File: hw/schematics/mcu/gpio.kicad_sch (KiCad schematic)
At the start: 5 parts

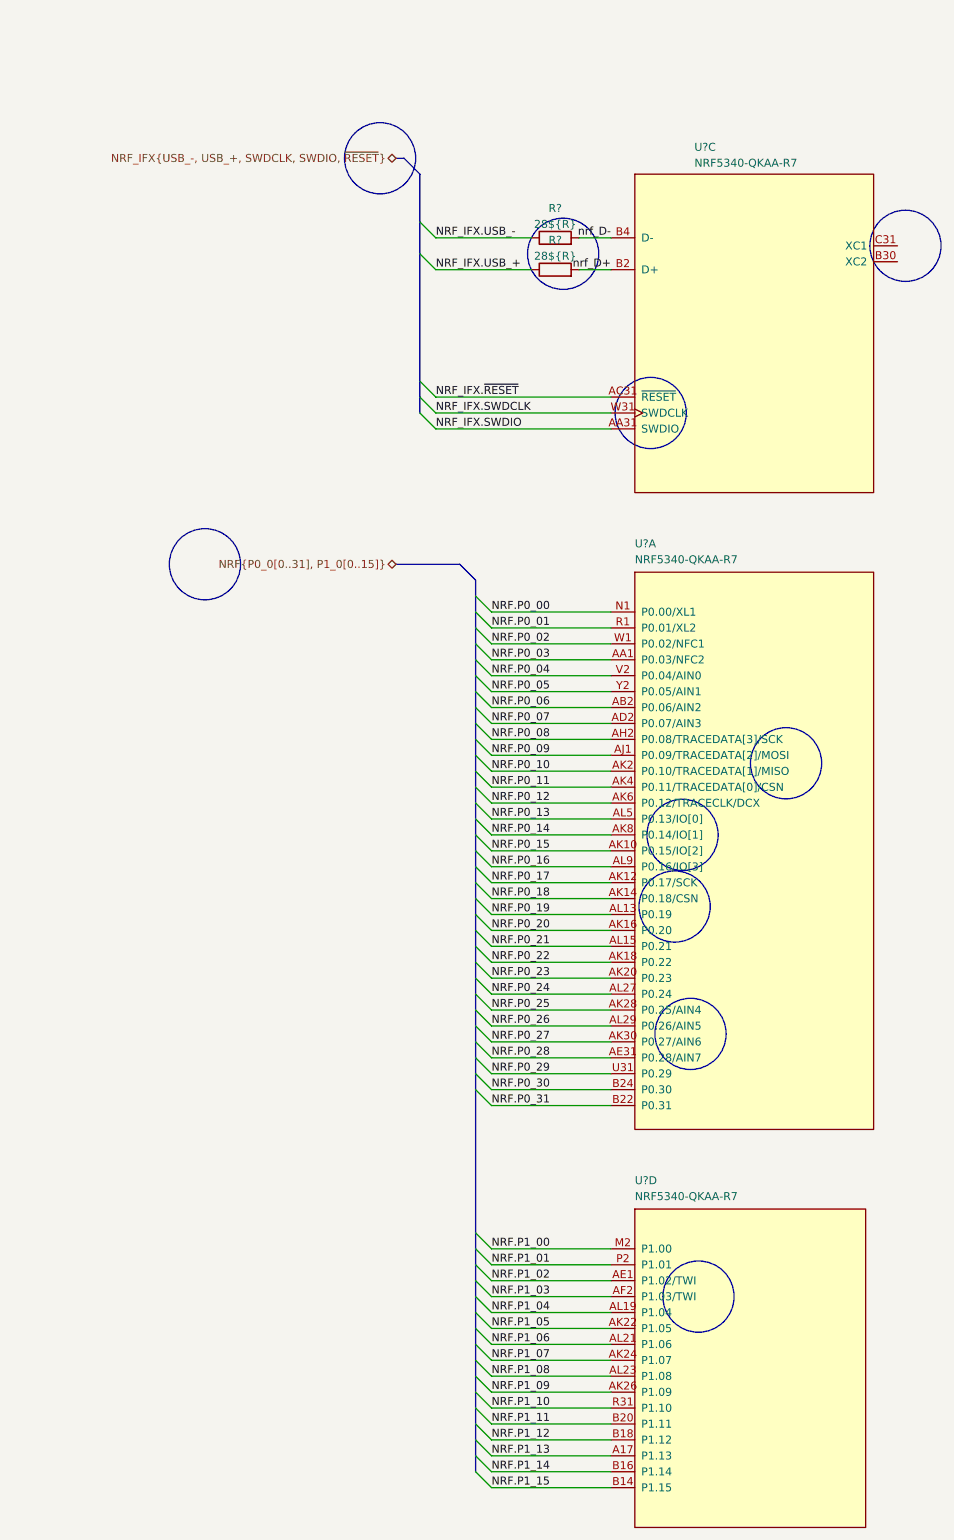
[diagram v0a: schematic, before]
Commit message: 
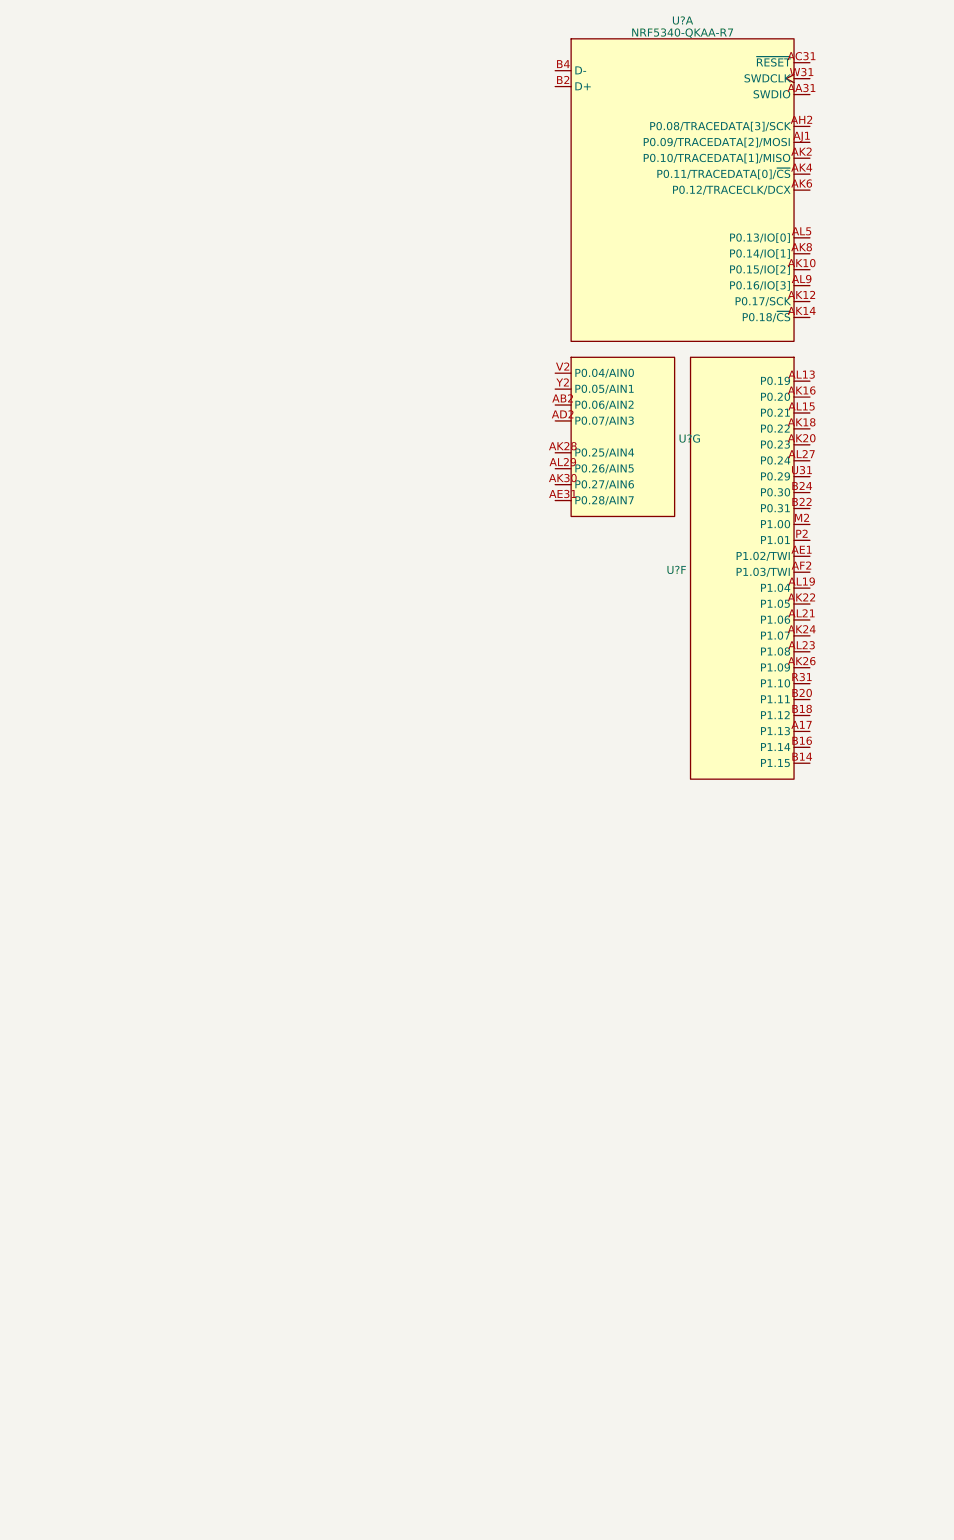
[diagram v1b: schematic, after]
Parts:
- removed R? (x2): 28${R}, Resistor_SMD:R_0201_0603Metric, symbol Device:R
- removed U? (x3): NRF5340-QKAA-R7, 0:NRF5340-QKAA-R7, symbol 1.Embedded.Specialized:NRF5340-QKAA-R7
- added U? (x3): NRF5340-QKAA-R7, 0:NRF5340-QKAA-R7, symbol 1.Embedded.Specialized:NRF5340-QKAA-R7
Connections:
- new net: U?.A1 (NC), U?.A31 (NC), U?.AG31 (NC), U?.AL1 (NC), U?.AL31 (NC), U?.D2 (NC), U?.F2 (NC), U?.K2 (NC), U?.T2 (NC)
